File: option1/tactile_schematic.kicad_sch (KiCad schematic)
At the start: 28 parts, among them IC1 CY8C4145PVI-PS431, J1 Conn_01x02, J2 Conn_01x04

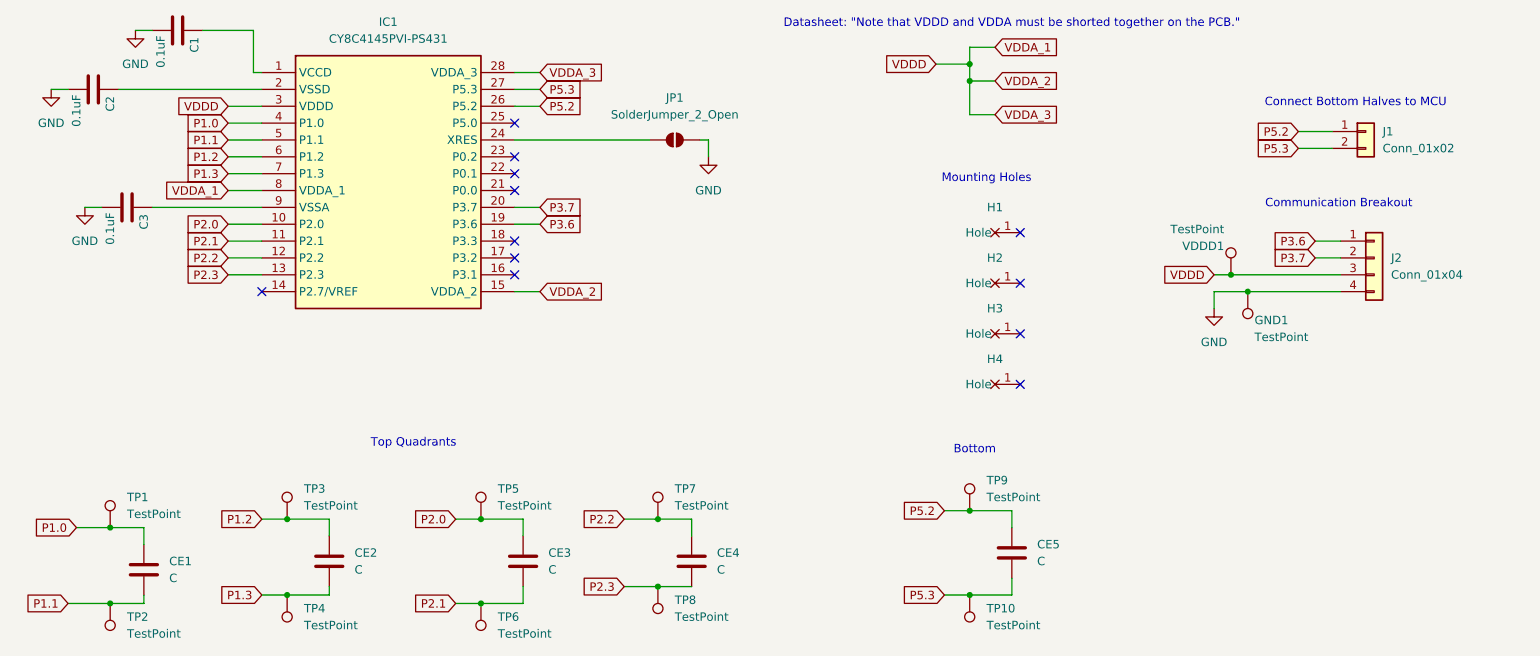
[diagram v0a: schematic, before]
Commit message: need to fix edge cuts not lining up
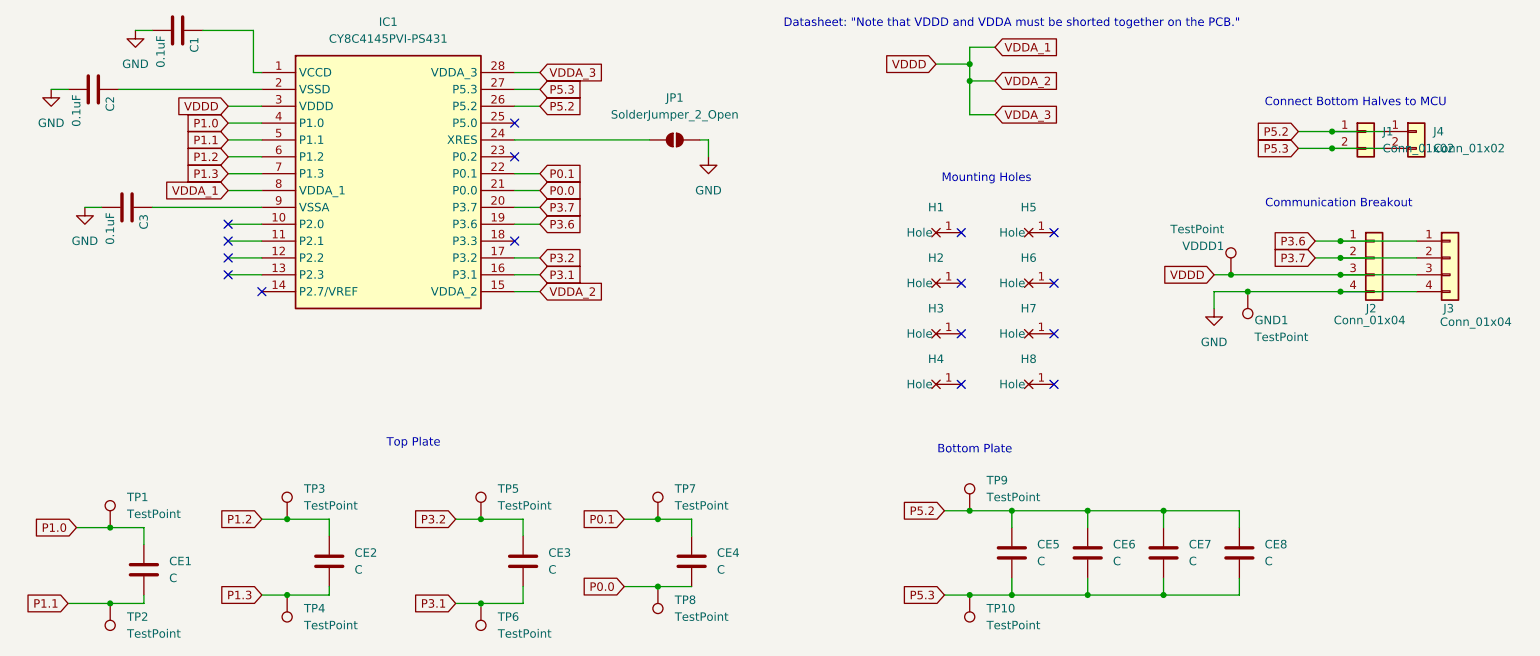
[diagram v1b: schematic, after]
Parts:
- added CE6, CE7, CE8: C, PCB Coils:COIL_GENERATOR, symbol ECE445L:C
- added H5, H6, H7, H8: ~, ECE445L:MountingHole_4_40, symbol ECE445L:MountingHole
- added J3: Conn_01x04, Connector_JST:JST_SH_SM03B-SRSS-TB_1x03-1MP_P1.00mm_Horizontal, symbol Connector_Generic:Conn_01x04
- added J4: Conn_01x02, Connector_PinHeader_2.00mm:PinHeader_1x02_P2.00mm_Vertical, symbol Connector_Generic:Conn_01x02
- CE1, CE2, CE3, CE4: footprint ECE382N:E1 -> PCB Coils:COIL_GENERATOR
- CE5: footprint ECE382N:Bottom_Electrode -> PCB Coils:COIL_GENERATOR
- IC1: footprint SOP65P780X200-28N -> ECE382N:SOP65P780X200-28N
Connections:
- net GND: now also J3.4 (Pin_4)
- net P3.6: now also J3.1 (Pin_1)
- net P3.7: now also J3.2 (Pin_2)
- net P5.2: now also CE6.1, CE7.1, CE8.1, J4.1 (Pin_1)
- net P5.3: now also CE6.2, CE7.2, CE8.2, J4.2 (Pin_2)
- net VDDA_1: now also J3.3 (Pin_3)
- net P3.1: now reaches IC1.16 (P3.1)
- net P3.1: now also CE3.2, TP6.1
- net P3.2: now reaches IC1.17 (P3.2)
- net P3.2: now also CE3.1, TP5.1
- net P0.0: now reaches IC1.21 (P0.0)
- net P0.0: now also CE4.2, TP8.1
- net P0.1: now reaches IC1.22 (P0.1)
- net P0.1: now also CE4.1, TP7.1
- removed net P2.0: CE3.1, IC1.10 (P2.0), TP5.1
- removed net P2.1: CE3.2, IC1.11 (P2.1), TP6.1
- removed net P2.2: CE4.1, IC1.12 (P2.2), TP7.1
- removed net P2.3: CE4.2, IC1.13 (P2.3), TP8.1
- no-connect marks 12 -> 16
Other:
- note added: "Bottom Plate"
- note added: "Top Plate"
- note removed: "Bottom"
- note removed: "Top Quadrants"
- moved on the sheet: H1, H2, H3, H4
